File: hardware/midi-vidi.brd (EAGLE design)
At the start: 152.5 x 43.6 mm, 82 parts, among them IC1 MAX4311SO14, IC2 PIC16F1825SO14, IC3 74HC595D, IC4 4051D, IC5 MAX4311SO14, IC6 REG1117, IC7 74HC595D, IC8 B1S

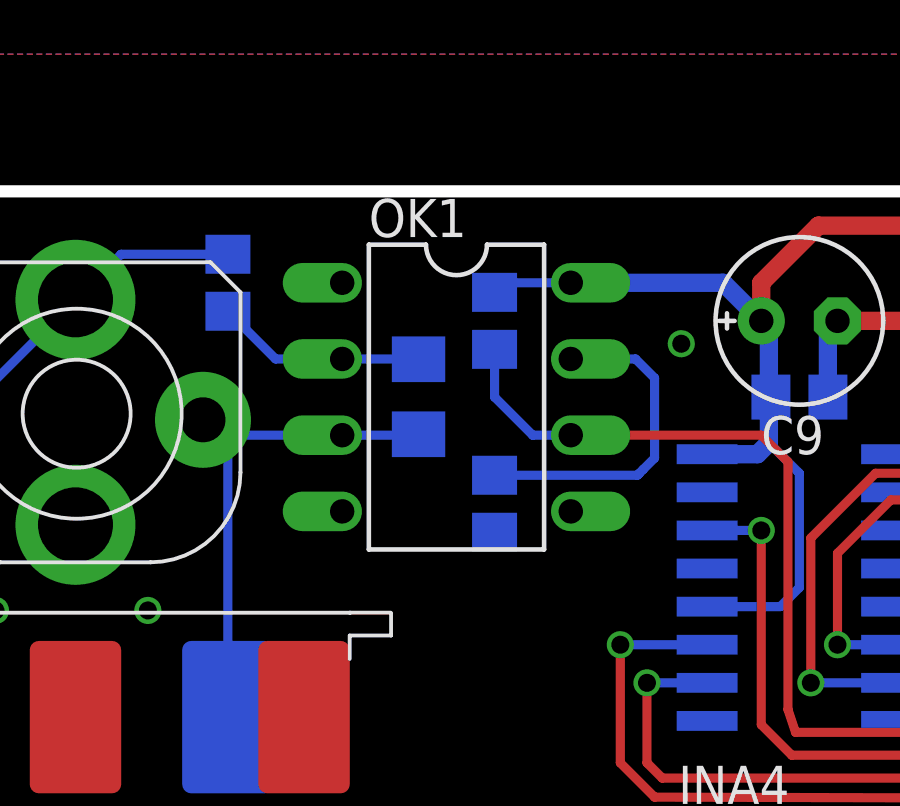
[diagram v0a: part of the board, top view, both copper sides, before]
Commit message: Fix DRC issues - FINAL REV 1 PCB
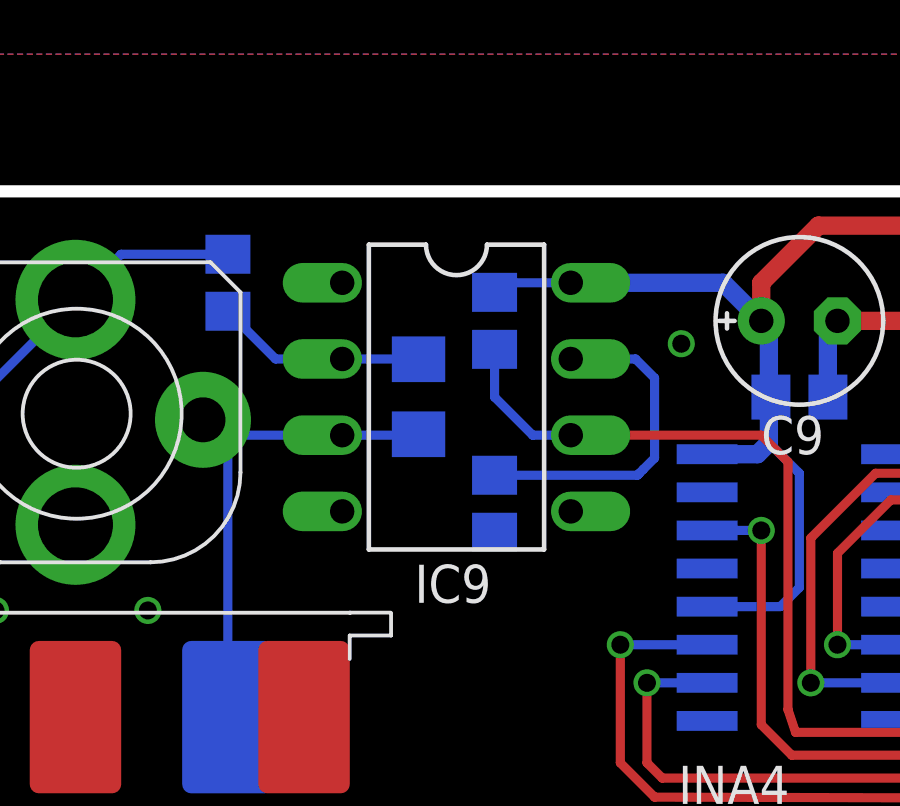
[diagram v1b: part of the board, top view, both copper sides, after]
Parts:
- renumbered OK1 to IC9
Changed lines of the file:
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@@
 </class>
 </classes>
-<designrules name="ITEADstudio_DRC">
-<description language="de">&lt;b&gt;EAGLE Design Rules&lt;/b&gt;
+<designrules name="hackvana">
+<description language="de">&lt;b&gt;EAGLE Design Rules für Hackvana&lt;/b&gt;
 &lt;p&gt;
 Die Standard-Design-Rules sind so gewählt, dass sie für
@@
 Einstellungen hier und speichern die Design Rules unter
 einem neuen Namen ab.</description>
-<description language="en">&lt;b&gt;EAGLE Design Rules&lt;/b&gt;
+<description language="en">&lt;b&gt;EAGLE Design Rules for Hackvana&lt;/b&gt;
 &lt;p&gt;
 The default Design Rules have been set to cover
@@
 necessary adjustments and save your customized
 design rules under a new name.</description>
-<description language="zh">&lt;b&gt;Seeed Studio EAGLE Design Rules&lt;/b&gt;
+<description language="zh">&lt;b&gt;EAGLE Design Rules for Hackvana&lt;/b&gt;
 </description>
 <param name="layerSetup" value="(1*16)"/>
@@
 <param name="mtIsolate" value="1.5mm 0.15mm 0.2mm 0.15mm 0.2mm 0.15mm 0.2mm 0.15mm 0.2mm 0.15mm 0.2mm 0.15mm 0.2mm 0.15mm 0.2mm"/>
 <param name="mdWireWire" value="6mil"/>
-<param name="mdWirePad" value="6mil"/>
+<param name="mdWirePad" value="9mil"/>
 <param name="mdWireVia" value="6mil"/>
 <param name="mdPadPad" value="6mil"/>
@@
 <param name="mdViaViaSameLayer" value="8mil"/>
 <param name="mnLayersViaInSmd" value="2"/>
-<param name="mdCopperDimension" value="10mil"/>
-<param name="mdDrill" value="10mil"/>
+<param name="mdCopperDimension" value="6mil"/>
+<param name="mdDrill" value="6mil"/>
 <param name="mdSmdStop" value="0mil"/>
 <param name="msWidth" value="6mil"/>
-<param name="msDrill" value="12mil"/>
-<param name="msMicroVia" value="12mil"/>
+<param name="msDrill" value="0.3mm"/>
+<param name="msMicroVia" value="0.25mm"/>
 <param name="msBlindViaRatio" value="0.5"/>
 <param name="rvPadTop" value="0.25"/>
@@
 <attribute name="VALUE" x="52.07" y="38.1" size="1.27" layer="28" rot="MR90"/>
 </element>
-<element name="OK1" library="optocoupler" package="DIL08" value="6N138" x="29.21" y="35.56" smashed="yes" rot="R270">
+<element name="IC9" library="optocoupler" package="DIL08" value="6N138" x="29.21" y="35.56" smashed="yes" rot="R270">
 <attribute name="OC_NEWARK" value="35K5294" x="29.21" y="35.56" size="1.778" layer="27" rot="R270" display="off"/>
 <attribute name="MPN" value="6N138" x="29.21" y="35.56" size="1.778" layer="27" rot="R270" display="off"/>
 <attribute name="MF" value="VISHAY/TELEFUNKEN" x="29.21" y="35.56" size="1.778" layer="27" rot="R270" display="off"/>
 <attribute name="OC_FARNELL" value="9860150" x="29.21" y="35.56" size="1.778" layer="27" rot="R270" display="off"/>
-<attribute name="NAME" x="26.289" y="40.894" size="1.27" layer="25" ratio="10"/>
-<attribute name="VALUE" x="28.575" y="39.116" size="1.27" layer="27" ratio="10" rot="R270"/>
+<attribute name="NAME" x="27.813" y="28.702" size="1.27" layer="25" ratio="10"/>
 </element>
 <element name="D1" library="jasons_stuff" package="0805DIODE" value="0805DIODE" x="27.94" y="35.56" smashed="yes" rot="MR270">
@@
 <contactref element="IC1" pad="11"/>
 <contactref element="C6" pad="2"/>
-<contactref element="OK1" pad="5"/>
+<contactref element="IC9" pad="5"/>
 <contactref element="R20" pad="1"/>
 <contactref element="LED2" pad="K"/>
@@
 <contactref element="C6" pad="1"/>
 <contactref element="IC1" pad="4"/>
-<contactref element="OK1" pad="8"/>
+<contactref element="IC9" pad="8"/>
 <contactref element="R19" pad="1"/>
 <contactref element="C8" pad="2"/>
@@
 </signal>
 <signal name="N$8">
-<contactref element="OK1" pad="2"/>
+<contactref element="IC9" pad="2"/>
 <contactref element="D1" pad="A"/>
 <contactref element="R21" pad="1"/>
@@
 </signal>
 <signal name="N$18">
-<contactref element="OK1" pad="3"/>
+<contactref element="IC9" pad="3"/>
 <contactref element="D1" pad="C"/>
 <contactref element="MIDI_IN" pad="5"/>
@@
 </signal>
 <signal name="MIDI">
-<contactref element="OK1" pad="6"/>
+<contactref element="IC9" pad="6"/>
 <contactref element="R19" pad="2"/>
 <contactref element="IC2" pad="5"/>
@@
 </signal>
 <signal name="N$22">
-<contactref element="OK1" pad="7"/>
+<contactref element="IC9" pad="7"/>
 <contactref element="R20" pad="2"/>
 <wire x1="33.02" y1="36.83" x2="35.179" y2="36.83" width="0.3048" layer="16"/>

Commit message: updates - working for rev2
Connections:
- net ST_CLK: now also IC3.12, IC7.12; no longer IC3.10, IC7.10
- net VCC: now also IC3.10, IC7.10; no longer IC3.12, IC7.12
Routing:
- net ST_CLK: track 82.8 -> 88.6 mm
- net SH_CLK: track 86.7 -> 85.7 mm
- net NSHDNA: track 47.6 -> 48.4 mm
- net AD0: track 39.1 -> 39.9 mm
- net DAT: track 27.9 -> 27.4 mm
- net N$23: vias 0 -> 2
- net GND: vias 9 -> 11
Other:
- board text added: "rev 2"
- board text removed: "rev 1"
